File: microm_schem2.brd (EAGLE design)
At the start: 94 x 91.5 mm, 77 parts, among them Q1 16 MHz, T1 SIP32432DR3-T1GE3

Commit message: Add changes from meeting today.
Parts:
- removed C8: 100nF, rcl:C0805
- removed LED3, LED4: red, 20mA, 2.5V, led:CHIPLED_0805
- removed R11, R7: 47Ω, rcl:R0805
- removed R2: 1kΩ, rcl:R0805
- removed R3: 10kΩ, rcl:R0805
- removed S2: TS04-66-95-BK-160-SMT-TR, SamacSys_Parts:TS046695BK160SMTTR
- removed T1: SIP32432DR3-T1GE3, SamacSys_Parts:SOT65P210X110-6N
- added BT_RST: (no value), pinhead:1X02
- added RX_SEL: (no value), pinhead:1X03
- renumbered RESET to µC_RST
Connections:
- removed net BUTTON2: R2.2
- removed net LED3: LED3.C
- removed net LED4: LED4.C
- removed net N$1: C8.1, R2.1, R3.1, S2.2, S2.4
- removed net N$10: LED4.A, R11.2
- removed net N$9: LED3.A, R7.2
- removed net SENS_DIST_ON: T1.3, UC.32
- removed net SENS_DIST_V: C12.1, C13.1, C14.1, SENS_DIST_1.1, SENS_DIST_2.1, SENS_DIST_3.1, T1.1
- new net UART_BT_RX: RX_SEL.1, UART_BT.7
- new net UART_DBG_RX: RX_SEL.3, UART.1
- net +3V3: no longer R11.1, R3.2, R7.1
- net +5V: now also C12.1, C13.1, C14.1, SENS_DIST_1.1, SENS_DIST_2.1, SENS_DIST_3.1; no longer T1.4
- net BT_RESET: now also BT_RST.1
- net GND: now also BT_RST.2; no longer C8.2, S2.1, S2.3, T1.2, T1.5
- net UART_RX: now also RX_SEL.2; no longer UART.1, UART_BT.7

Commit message: Update schematic.
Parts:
- removed BT_STATUS: blue, 20mA, 3.3V, led:CHIP-LED0805
- removed PROGRAM: (no value), pinhead:1X06/90
- removed R14: 0Ω, rcl:R0805
- removed TP3V3, TP5V, TP7V4, TPGND, TP_OSC: (no value), pinhead:1X01
- added BT_CON: blue, 2mA, 3V, led:CHIP-LED0805
- added BT_PROG: (no value), pinhead:1X02
- added C8: 10uF, rcl:C0805
- added H3, H4, H5, H6, H7, H8: MOUNT-PAD-ROUND2.8, holes:2,8-PAD
- added L1: 47uH, rcl:L1812
- added R11: 1kΩ, rcl:R0805
- added R2: 1.2kΩ, rcl:R0805
- added R3: 180Ω, rcl:R0805
- added R7: 2.2kΩ, rcl:R0805
- added T3.3V, T5V, T7.4V, TGND: (no value), pinhead:1X01
- added UC_PROG: (no value), pinhead:1X06/90
- 3.3V, 5V, 7.4V: value green, 20mA, 2.5V -> green, 2mA, 3V
- C12, C13, C14: value 10 uF -> 100nF, 10-20V, low-esr
- C15, C16: value 100nF, 10-20V, low-esr -> 20pF, low-esr, ceramic
- C17, C18: value 20pF, low-esr, ceramic -> 10 uF
- C19: value 100nF -> 10 uF
- C20: value 10uF -> 1uF
- C21: value 100nF, 10-20V, low-esr -> 1uF
- C22: value 100nF, 10-20V, low-esr -> 100nF
- C3: value 100nF -> 10uF, tantalum
- C4: value 10uF, tantalum -> 22uF, tantalum, esr 0.3-22Ω
- C5: value 22uF, tantalum, esr 0.3-22Ω -> 100nF
- C6: value 100nF -> 10uF
- C7: value 10uF -> 100nF
- C9: value 1uF -> 100nF, 10-20V, low-esr
- LED1, LED2: value red, 20mA, 2.5V -> red, 2mA, 2.1V
- R1: value 270Ω -> 2.7kΩ
- R12: value 150Ω -> 10kΩ
- R13: value 47Ω -> 10kΩ
- R4: value 10kΩ -> 680Ω
- R5: value 47Ω -> 680Ω
- R6: value 47Ω -> 180Ω
- R8: value 1kΩ -> 2.2kΩ
- moved BT_RST 194.3 mm to (29.2, 15.2)
- moved RX_SEL 184.8 mm to (21.6, 17.8), turned to 270 degrees
- moved H1 98.1 mm to (25.4, -38.7)
- moved H2 98.1 mm to (25.4, -65.4)
- moved LCD 98.1 mm to (2.54, -52.1)
- moved C17 83.5 mm to (86.4, 73.0), turned to 0 degrees
- moved C13 71.0 mm to (15.4, 18.0)
- moved R6 67.3 mm to (20.3, 8.89), turned to 0 degrees
- moved C19 63.7 mm to (86.4, 8.26), turned to 0 degrees
- moved C12 63.4 mm to (15.1, 57.4), turned to 90 degrees
- moved C18 60.7 mm to (93.3, 39.4)
- moved C5 59.7 mm to (16.5, 41.9)
- moved R13 57.2 mm to (35.6, 15.2), turned to 0 degrees
- moved LED2 57.1 mm to (43.2, 3.81), turned to 270 degrees
- moved R12 55.9 mm to (35.6, 20.3), turned to 0 degrees
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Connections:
- removed net AGND: R14.2, UC.16
- removed net N$11: C4.1, VR_3.3V.1
- removed net N$13: C1.1, VR_5V.1
- new net BT_PROG: BT_PROG.1, C21.1, R12.1, UART_BT.16
- new net N$1: BT_CON.A, R6.2
- new net N$5: C14.2, L1.1, UC.17
- new net UART_BT_RX_IND: UART_BT.6
- net +3V3: now also BT_CON.C, C12.1, C13.1, C4.1, C7.1, C8.1, C9.1, L1.2, R10.2, R12.2, R13.2, R3.1, R4.1, R7.1, R8.1, T3.3V.1, UC_PROG.2; no longer BT_STATUS.C, C15.1, C16.1, C19.1, C20.1, C21.1, C22.1, C5.1, PROGRAM.2, R13.1, R4.2, R6.1, R9.2, TP3V3.1, UC.17
- net +5V: now also C17.1, C18.1, C19.1, C3.1, R2.1, T5V.1; no longer C12.1, C13.1, C14.1, R12.1, TP5V.1
- net +7V4: now also C1.1, C5.1, T7.4V.1; no longer C7.1, TP7V4.1
- net BT_RESET: now also C20.1, R13.1; no longer C9.1, R4.1
- net BT_STATUS: now also R6.1; no longer BT_STATUS.A
- net BUTTON1: now also R11.2; no longer R8.2
- net GND: now also BT_PROG.2, C14.1, C8.2, H3.B2,8, H4.B2,8, H5.B2,8, H6.B2,8, H7.B2,8, H8.B2,8, TGND.1, UC.16, UC_PROG.3, VR_3.3V.1, VR_5V.1; no longer C14.2, PROGRAM.3, R14.1, TPGND.1
- net I2C_SCL: now also R7.2
- net I2C_SDA: now also R8.2
- net MCLR: now also R9.1, UC_PROG.1; no longer PROGRAM.1, R10.1
- net N$16: now also R2.2; no longer R12.2
- net N$17: now also R3.2; no longer R13.2
- net N$3: now also R4.2; no longer R5.2
- net N$6: now also C22.1, R10.1, R11.1; no longer C3.1, R8.1, R9.1
- net N$7: now also R9.2; no longer R10.2
- net N$8: now also R5.2; no longer R6.2
- net OSC1: now also C15.1; no longer C17.1
- net OSC2: now also C16.1; no longer C18.1, TP_OSC.1
- net PG_EC1: now also UC_PROG.5; no longer PROGRAM.5
- net PG_ED1: now also UC_PROG.4; no longer PROGRAM.4
- net UART_BT_RX: now also UART_BT.8; no longer UART_BT.7
- net UART_TX: now also UART_BT.7; no longer UART_BT.8
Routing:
- added copper zone on layer 16, net GND
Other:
- board size 94 x 91.5 mm -> 101.6 x 81.3 mm

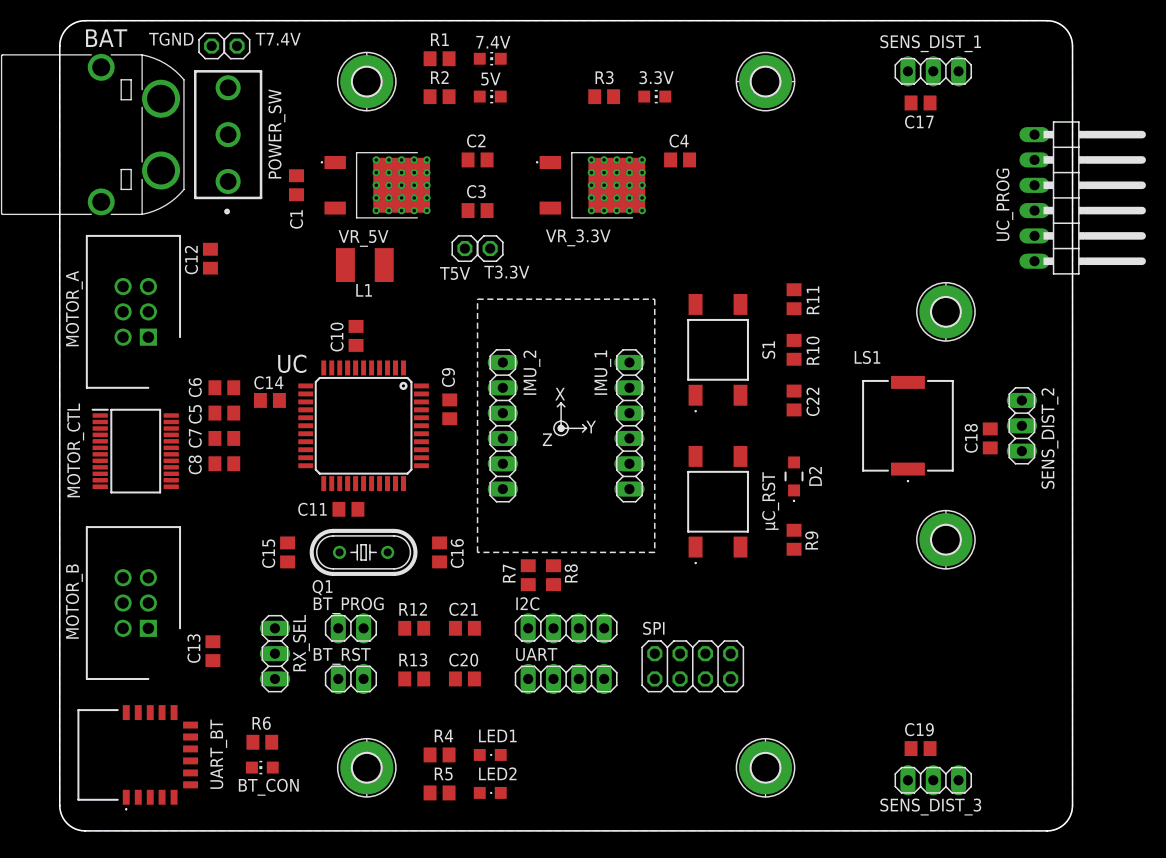
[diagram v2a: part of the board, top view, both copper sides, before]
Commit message: WIP: Trace the airwires
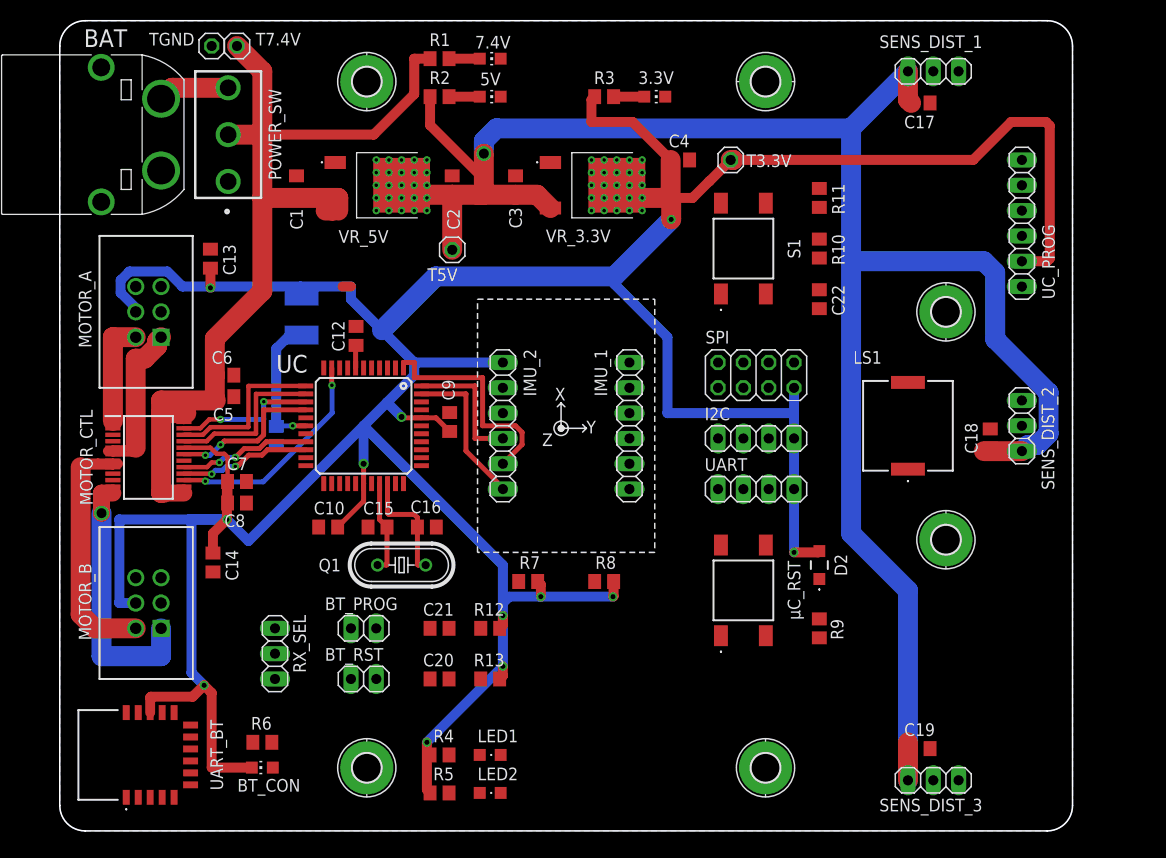
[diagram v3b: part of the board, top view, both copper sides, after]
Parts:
- C12: value 100nF, 10-20V, low-esr -> 10uF, 10-20V, low-esr
- UC_PROG: device pinhead:1X06/90 -> pinhead:1X06
- moved C13 39.4 mm to (15.1, 57.4)
- moved SPI 29.9 mm to (69.8, 45.7)
- moved I2C 26.9 mm to (69.8, 39.4)
- moved UART 26.9 mm to (69.8, 34.3)
- moved T3.3V 25.7 mm to (67.3, 67.3)
- moved C10 19.4 mm to (26.9, 30.5), turned to 180 degrees
- moved C14 17.2 mm to (15.4, 26.9), turned to 270 degrees
- moved C12 16.5 mm to (29.7, 49.7), turned to 270 degrees
- moved C22 10.5 mm to (76.2, 53.3)
- moved R10 10.5 mm to (76.2, 58.4)
- moved S1 10.5 mm to (68.6, 58.4)
- moved R11 10.5 mm to (76.2, 63.5)
- moved C11 10.3 mm to (21.7, 39.6), flipped to the bottom, turned to 90 degrees
- moved C15 9.37 mm to (31.9, 30.5), turned to 180 degrees
- moved D2 9.25 mm to (76.2, 26.7)
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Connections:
- new net VCAP/VDDCORE: C12.2, UC.7
- net +3V3: now also C14.1; no longer C11.1, C12.1, UC.7
- net GND: now also C11.1, C12.1, C14.2; no longer C11.2, C12.2, C14.1
- net LED1: now also UC.34; no longer UC.19
- net LED2: now also UC.35; no longer UC.20
- net MA_DIR1: now also UC.13; no longer UC.12
- net MA_DIR2: now also UC.12; no longer UC.13
- net MB_DIR1: now also UC.19; no longer UC.34
- net MB_DIR2: now also UC.20; no longer UC.35
- net M_STDBY: now also UC.15; no longer UC.38
- net N$5: now also C11.2; no longer C14.2
- net SPI_SDO: now also UC.38; no longer UC.15
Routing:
- net +3V3: track 0.00 -> 403.8 mm, vias 0 -> 12
- net +5V: track 0.00 -> 200.0 mm, vias 0 -> 1
- net +7V4: track 0.00 -> 95.5 mm
- net MB_OUT2: track 0.00 -> 33.1 mm
- net MB_OUT1: track 0.00 -> 26.9 mm, vias 0 -> 1
- net I2C_SDA: track 0.00 -> 23.0 mm
- net MB_PWM: track 0.00 -> 22.3 mm, vias 0 -> 2
- net MA_OUT2: track 0.00 -> 20.1 mm
- net MA_DIR2: track 0.00 -> 16.7 mm
- net MA_DIR1: track 0.00 -> 16.5 mm
- net M_STDBY: track 0.00 -> 15.6 mm, vias 0 -> 2
- net IMU_INT: track 0.00 -> 15.6 mm
- net MA_PWM: track 0.00 -> 14.4 mm, vias 0 -> 2
- net I2C_SCL: track 0.00 -> 13.4 mm
- net MB_DIR2: track 0.00 -> 13.3 mm, vias 0 -> 2
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
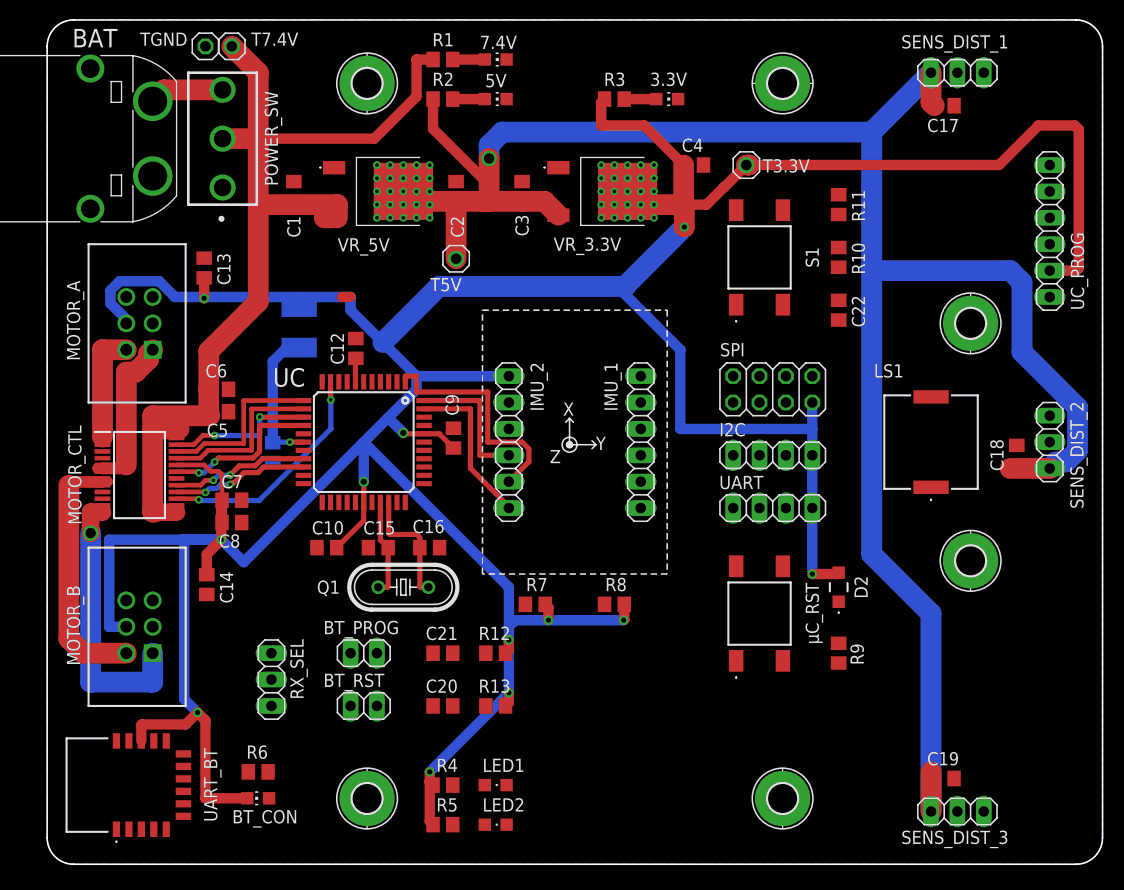
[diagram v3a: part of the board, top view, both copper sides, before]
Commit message: Improve 3.3V routing.
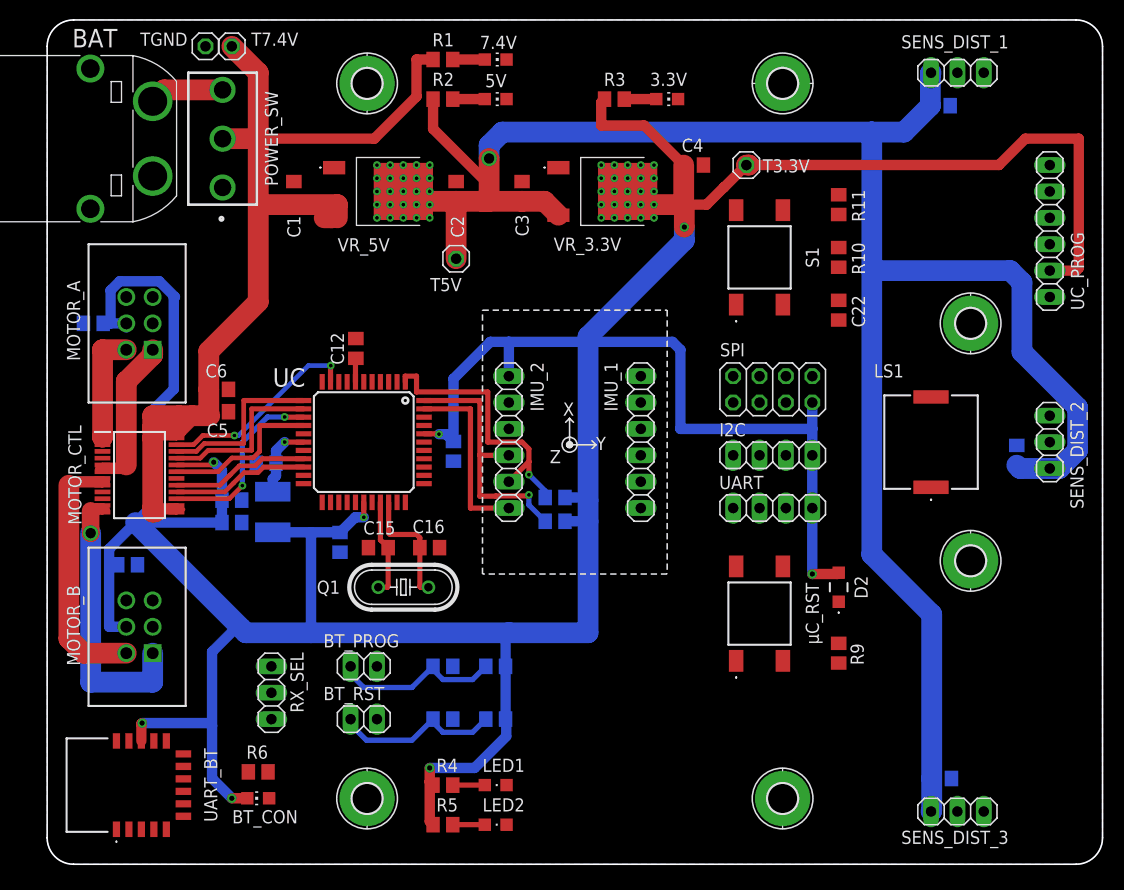
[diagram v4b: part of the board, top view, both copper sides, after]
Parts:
- S1, µC_RST: value TS04-66-95-BK-160-SMT-TR -> TS04-66-50-BK-100-SMT-TR; device SamacSys_Parts:TS046695BK160SMTTR -> SamacSys_Parts:TS046650BK100SMTTR
- moved L1 18.0 mm to (21.7, 33.9), turned to 270 degrees
- moved C13 11.9 mm to (4.45, 52.1), flipped to the bottom, turned to 0 degrees
- moved R8 11.8 mm to (48.9, 35.3), flipped to the bottom, turned to 0 degrees
- moved R7 8.22 mm to (48.9, 33.0), flipped to the bottom, turned to 0 degrees
- moved C14 7.85 mm to (7.75, 28.8), flipped to the bottom, turned to 180 degrees
- moved C10 1.37 mm to (28.2, 31.0), flipped to the bottom, turned to 270 degrees
- moved C9 1.27 mm to (39.1, 39.8), flipped to the bottom, turned to 270 degrees
- moved BT_PROG 1.27 mm to (30.5, 19.1)
- moved BT_RST 1.27 mm to (30.5, 14.0)
- moved C20 1.27 mm to (38.1, 14.0), flipped to the bottom, turned to 180 degrees
- moved C21 1.27 mm to (38.1, 19.1), flipped to the bottom, turned to 180 degrees
- moved R12 1.27 mm to (43.2, 19.1), flipped to the bottom, turned to 180 degrees
- moved R13 1.27 mm to (43.2, 14.0), flipped to the bottom, turned to 180 degrees
- moved RX_SEL 1.27 mm to (21.6, 16.5)
- moved C11 1.20 mm to (21.1, 38.6), turned to 180 degrees
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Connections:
- net MA_PWM: now also UC.10; no longer UC.14
- net MB_PWM: now also UC.14; no longer UC.10
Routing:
- net BT_PROG: track 0.00 -> 16.6 mm
- net BT_RESET: track 0.00 -> 16.5 mm
- net I2C_SCL: track 13.4 -> 25.3 mm, vias 0 -> 1
- net +7V4: track 95.5 -> 106.2 mm
- net +3V3: track 403.8 -> 394.0 mm, vias 12 -> 8
- net +5V: track 200.0 -> 194.2 mm
- net N$5: track 12.4 -> 7.07 mm
- net MA_PWM: track 14.4 -> 19.6 mm
- net MB_PWM: track 22.3 -> 18.0 mm
- net I2C_SDA: track 23.0 -> 27.1 mm, vias 0 -> 1
- net N$8: track 0.00 -> 3.08 mm
- net N$3: track 0.00 -> 3.08 mm
- net MB_OUT1: track 26.9 -> 29.9 mm
- net IMU_INT: track 15.6 -> 17.7 mm
- net MA_OUT1: track 12.4 -> 11.4 mm
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
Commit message: Add most recent board version
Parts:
- removed H1, H2: MOUNT-PAD-ROUND2.8, holes:2,8-PAD
- removed LCD: (no value), pinhead:1X11
- removed SPI: (no value), pinhead:2X04
- moved RX_SEL 27.9 mm to (49.5, 16.5), turned to 90 degrees
- moved LED1 20.5 mm to (61.0, 17.8)
- moved LED2 20.5 mm to (61.0, 14.0)
- moved R4 19.4 mm to (54.6, 17.8)
- moved R5 19.4 mm to (54.6, 14.0)
- moved R11 12.0 mm to (66.0, 57.1), turned to 180 degrees
- moved R10 9.67 mm to (67.3, 62.2)
- moved C22 8.89 mm to (67.3, 53.3)
- moved R6 5.68 mm to (22.9, 3.81), turned to 270 degrees
- moved C19 5.24 mm to (91.2, 9.53)
- moved S1 5.08 mm to (73.7, 58.4), turned to 270 degrees
- moved BT_CON 2.84 mm to (19.1, 3.81), turned to 180 degrees
- moved C18 2.54 mm to (93.3, 41.9), turned to 270 degrees
- moved SENS_DIST_3 1.27 mm to (87.6, 3.81), turned to 180 degrees
- turned SENS_DIST_2 to 270 degrees
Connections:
- removed net LCD_BL_PWM: LCD.11, UC.8
- removed net LCD_RESET: LCD.8, UC.33
- removed net SPI_LCD_CS: LCD.7, SPI.2, UC.25
- removed net SPI_LCD_DC: LCD.9, UC.27
- removed net SPI_SCK: LCD.4, SPI.1, UC.9
- removed net SPI_SDI: LCD.6, SPI.5, UC.11
- removed net SPI_SDO: LCD.5, SPI.3, UC.38
- removed net SPI_SD_CS: LCD.10, SPI.4
- net +3V3: now also BT_CON.A; no longer BT_CON.C, LCD.1, SPI.7
- net GND: no longer H1.B2,8, H2.B2,8, LCD.3, SPI.8
- net MA_ENC_A: now also UC.4; no longer UC.36
- net MA_ENC_B: now also UC.5; no longer UC.37
- net MB_ENC_A: now also UC.24; no longer UC.4
- net MB_ENC_B: now also UC.23; no longer UC.5
- net N$1: now also BT_CON.C; no longer BT_CON.A
- net SENS_DIST_1: now also UC.25; no longer UC.23
- net SENS_DIST_2: now also UC.26; no longer UC.24
- net SENS_DIST_3: now also UC.27; no longer UC.26
- net UART_TX: now also UC.33; no longer UC.42
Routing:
- net MCLR: track 0.00 -> 134.7 mm, vias 0 -> 8
- net SENS_DIST_2: track 0.00 -> 126.8 mm, vias 0 -> 4
- net SENS_DIST_1: track 0.00 -> 115.1 mm, vias 0 -> 1
- net UART_TX: track 0.00 -> 102.1 mm, vias 0 -> 2
- net SENS_DIST_3: track 0.00 -> 98.5 mm, vias 0 -> 1
- net PG_ED1: track 0.00 -> 97.0 mm, vias 0 -> 2
- net PG_EC1: track 0.00 -> 96.6 mm, vias 0 -> 2
- net BUZZ_PWM: track 0.00 -> 69.8 mm
- net LED2: track 0.00 -> 42.0 mm, vias 0 -> 2
- net BUTTON1: track 0.00 -> 41.4 mm
- net UART_BT_RX: track 0.00 -> 39.3 mm, vias 0 -> 1
- net MA_ENC_A: track 0.00 -> 37.8 mm, vias 0 -> 2
- net LED1: track 0.00 -> 37.1 mm, vias 0 -> 2
- net UART_RX: track 0.00 -> 33.6 mm
- net I2C_SDA: track 27.1 -> 55.3 mm, vias 1 -> 2
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- added copper zone on layer 1, net GND
